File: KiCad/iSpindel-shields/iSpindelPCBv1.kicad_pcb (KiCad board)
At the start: 2 copper layers, 60 x 25 mm, 9 parts, among them SW1 SW_DPDT_x2, U1 GY-521, U2 LoRa_Ra-02, U3 WeMos_mini, U4 TP4056-shield-6PIN, U5 DS18B20

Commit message: adjust switch and charger
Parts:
- added SW2: SW_SPDT, KiCadCustomLibs:SS-12F23, F.Cu at (152.8, 112.5)
- SW1: value SW_DPDT_x2 -> SW_SPDT
- moved U4 0.75 mm to (146.2, 112.5)
- moved SW1 0.50 mm to (157.5, 112.5)

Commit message: adjusted some tracks
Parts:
- SW2: footprint KiCadCustomLibs:SS-12F23 -> SS-12F23
- moved U3 4.00 mm to (148.0, 112.5)
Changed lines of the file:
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@@
     (add_net "Net-(U4-Pad4)")
   )
-  (module KiCadCustomLibs:SS-12F23 (layer F.Cu)
+  (module KiCadCustomLibs:TP4056-shield-6PIN (layer B.Cu)
+    (at 146.25 112.5 180)
+    (fp_text reference U4 (at 0.5 0 180) (layer B.SilkS) hide
+      (effects (font (size 1 1) (thickness 0.15)) (justify mirror))
+    )
+    (fp_text value TP4056-shield-6PIN (at 0 7 180) (layer B.Fab) hide
+      (effects (font (size 1 1) (thickness 0.15)) (justify mirror))
+    )
+    (fp_line (start -14.5 -4) (end -9.5 -4) (layer B.Fab) (width 0.15))
+    (fp_line (start 13 6) (end 13 -6) (layer B.SilkS) (width 0.15))
+    (fp_line (start 13 6) (end 14.5 6) (layer B.SilkS) (width 0.15))
+    (fp_line (start 14.5 6) (end 14.5 8.5) (layer B.SilkS) (width 0.15))
+    (fp_line (start 14.5 8.5) (end 13.5 8.5) (layer B.SilkS) (width 0.15))
+    (fp_line (start 13 -6) (end 14.5 -6) (layer B.SilkS) (width 0.15))
+    (fp_line (start 14.5 -6) (end 14.5 -8.5) (layer B.SilkS) (width 0.15))
+    (fp_line (start 14.5 -8.5) (end 13.5 -8.5) (layer B.SilkS) (width 0.15))
+    (fp_line (start -9.5 -4) (end -9.5 4) (layer B.Fab) (width 0.15))
+    (fp_line (start -9.5 4) (end -14.5 4) (layer B.Fab) (width 0.15))
+    (fp_line (start -14.5 4) (end -14.5 -4) (layer B.Fab) (width 0.15))
+    (fp_line (start -13.5 -8.5) (end -13.5 8.5) (layer B.SilkS) (width 0.15))
+    (fp_line (start -13.5 8.5) (end 13.5 8.5) (layer B.SilkS) (width 0.15))
+    (fp_line (start 13.5 -8.5) (end -13.5 -8.5) (layer B.SilkS) (width 0.15))
+    (pad 3 thru_hole oval (at 11.1 7 180) (size 3 2) (drill 1) (layers *.Cu *.Mask)
+      (net 6 "Net-(SW1-Pad1)"))
+    (pad 4 thru_hole oval (at 11.1 -7 180) (size 3 2) (drill 1) (layers *.Cu *.Mask)
+      (net 28 "Net-(U4-Pad4)"))
+    (pad 2 thru_hole oval (at -11.5 -7 180) (size 3 2) (drill 1) (layers *.Cu B.Mask)
+      (net 13 GND))
+    (pad 1 thru_hole oval (at -11.5 7 180) (size 3 2) (drill 1) (layers *.Cu B.Mask)
+      (net 30 "Net-(U4-Pad1)"))
+    (model ../../../../../../src/Tennp/Git/KiCadCustomLibs/wrl/TP4056shield.wrl
+      (at (xyz 0 0 0))
+      (scale (xyz 0.395 0.395 0.395))
+      (rotate (xyz 0 0 180))
+    )
+    (model ../../../../../../src/Tennp/Git/KiCadCustomLibs/wrl/Conn_USB-micro-2.0_socket_right-angle.wrl
+      (at (xyz -0.47 0 0.047))
+      (scale (xyz 1 1 1))
+      (rotate (xyz 0 0 0))
+    )
+  )
+  (module SS-12F23 (layer F.Cu)
     (at 152.75 112.5 270)
     (fp_text reference SW2 (at 0.5 -2 270) (layer F.SilkS) hide
@@
     (pad 2 thru_hole circle (at 0 0 270) (size 2 2) (drill 1) (layers *.Cu *.Mask)
       (net 3 +5V))
+    (model ../../../../../../src/Tennp/Git/KiCadCustomLibs/wrl/SS-12F23.wrl
+      (at (xyz 0 0.12 0))
+      (scale (xyz 0.395 0.395 0.395))
+      (rotate (xyz 0 0 180))
+    )
   )
   (module wemos_D1_mini_board (layer F.Cu)
-    (at 144 112.5 90)
+    (at 148 112.5 90)
     (fp_text reference U3 (at -10.668 14.224 90) (layer F.SilkS)
       (effects (font (size 1 1) (thickness 0.15)))
@@
       (rotate (xyz 0 0 0))
     )
-  )
-  (module KiCadCustomLibs:TP4056-shield-6PIN (layer B.Cu)
-    (at 146.25 112.5 180)
-    (fp_text reference U4 (at 0.5 0 180) (layer B.SilkS)
-      (effects (font (size 1 1) (thickness 0.15)) (justify mirror))
-    )
-    (fp_text value TP4056-shield-6PIN (at 0 7 180) (layer B.Fab) hide
-      (effects (font (size 1 1) (thickness 0.15)) (justify mirror))
-    )
-    (fp_line (start -14.5 -4) (end -9.5 -4) (layer B.Fab) (width 0.15))
-    (fp_line (start 13 6) (end 13 -6) (layer B.SilkS) (width 0.15))
-    (fp_line (start 13 6) (end 14.5 6) (layer B.SilkS) (width 0.15))
-    (fp_line (start 14.5 6) (end 14.5 8.5) (layer B.SilkS) (width 0.15))
-    (fp_line (start 14.5 8.5) (end 13.5 8.5) (layer B.SilkS) (width 0.15))
-    (fp_line (start 13 -6) (end 14.5 -6) (layer B.SilkS) (width 0.15))
-    (fp_line (start 14.5 -6) (end 14.5 -8.5) (layer B.SilkS) (width 0.15))
-    (fp_line (start 14.5 -8.5) (end 13.5 -8.5) (layer B.SilkS) (width 0.15))
-    (fp_line (start -9.5 -4) (end -9.5 4) (layer B.Fab) (width 0.15))
-    (fp_line (start -9.5 4) (end -14.5 4) (layer B.Fab) (width 0.15))
-    (fp_line (start -14.5 4) (end -14.5 -4) (layer B.Fab) (width 0.15))
-    (fp_line (start -13.5 -8.5) (end -13.5 8.5) (layer B.SilkS) (width 0.15))
-    (fp_line (start -13.5 8.5) (end 13.5 8.5) (layer B.SilkS) (width 0.15))
-    (fp_line (start 13.5 -8.5) (end -13.5 -8.5) (layer B.SilkS) (width 0.15))
-    (pad 3 thru_hole oval (at 11.1 7 180) (size 3 2) (drill 1) (layers *.Cu *.Mask)
-      (net 6 "Net-(SW1-Pad1)"))
-    (pad 4 thru_hole oval (at 11.1 -7 180) (size 3 2) (drill 1) (layers *.Cu *.Mask)
-      (net 28 "Net-(U4-Pad4)"))
-    (pad 2 thru_hole oval (at -11.5 -7 180) (size 3 2) (drill 1) (layers *.Cu *.Mask)
-      (net 13 GND))
-    (pad 1 thru_hole oval (at -11.5 7 180) (size 3 2) (drill 1) (layers *.Cu *.Mask)
-      (net 30 "Net-(U4-Pad1)"))
-    (model ../../../../../../src/Tennp/Git/KiCadCustomLibs/wrl/TP4056shield.wrl
-      (at (xyz 0 0 0))
-      (scale (xyz 0.395 0.395 0.395))
-      (rotate (xyz 0 0 180))
-    )
-    (model ../../../../../../src/Tennp/Git/KiCadCustomLibs/wrl/Conn_USB-micro-2.0_socket_right-angle.wrl
-      (at (xyz -0.47 0 0.047))
-      (scale (xyz 1 1 1))
-      (rotate (xyz 0 0 0))
-    )

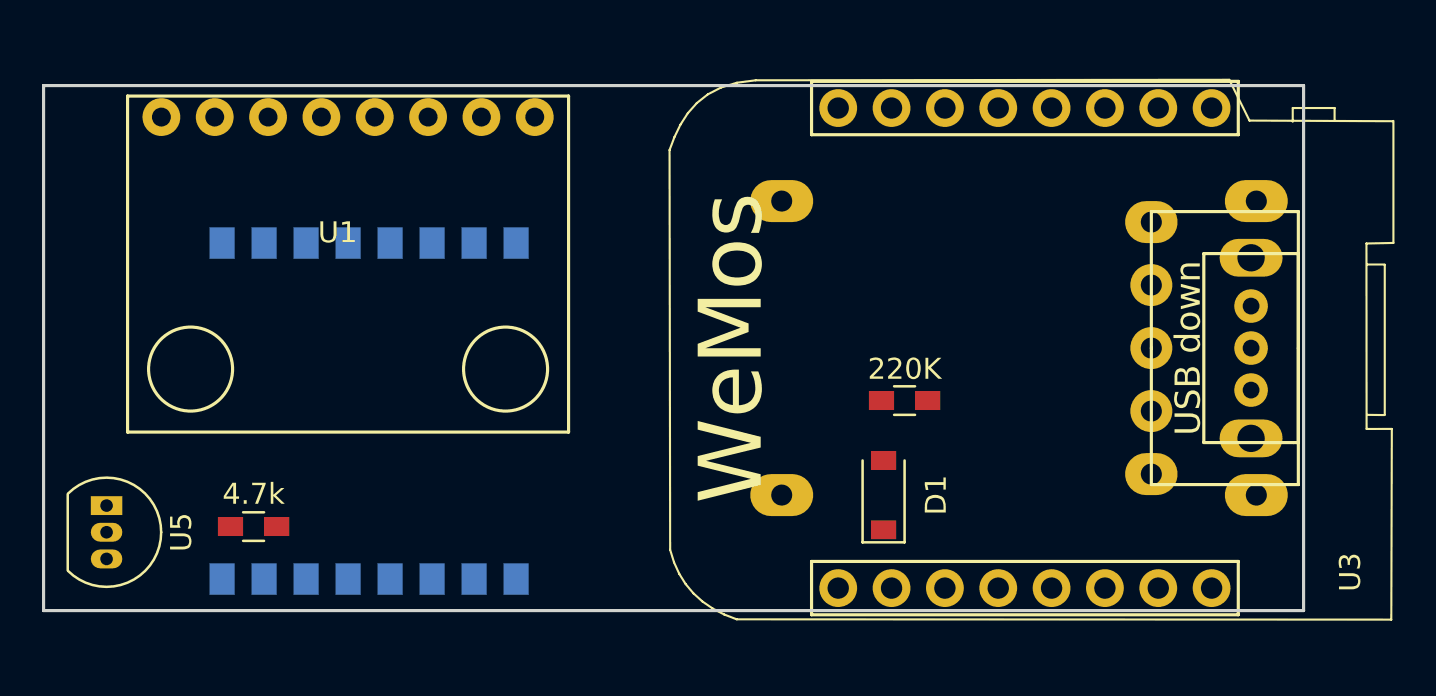
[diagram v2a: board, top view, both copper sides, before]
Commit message: Add TH variant
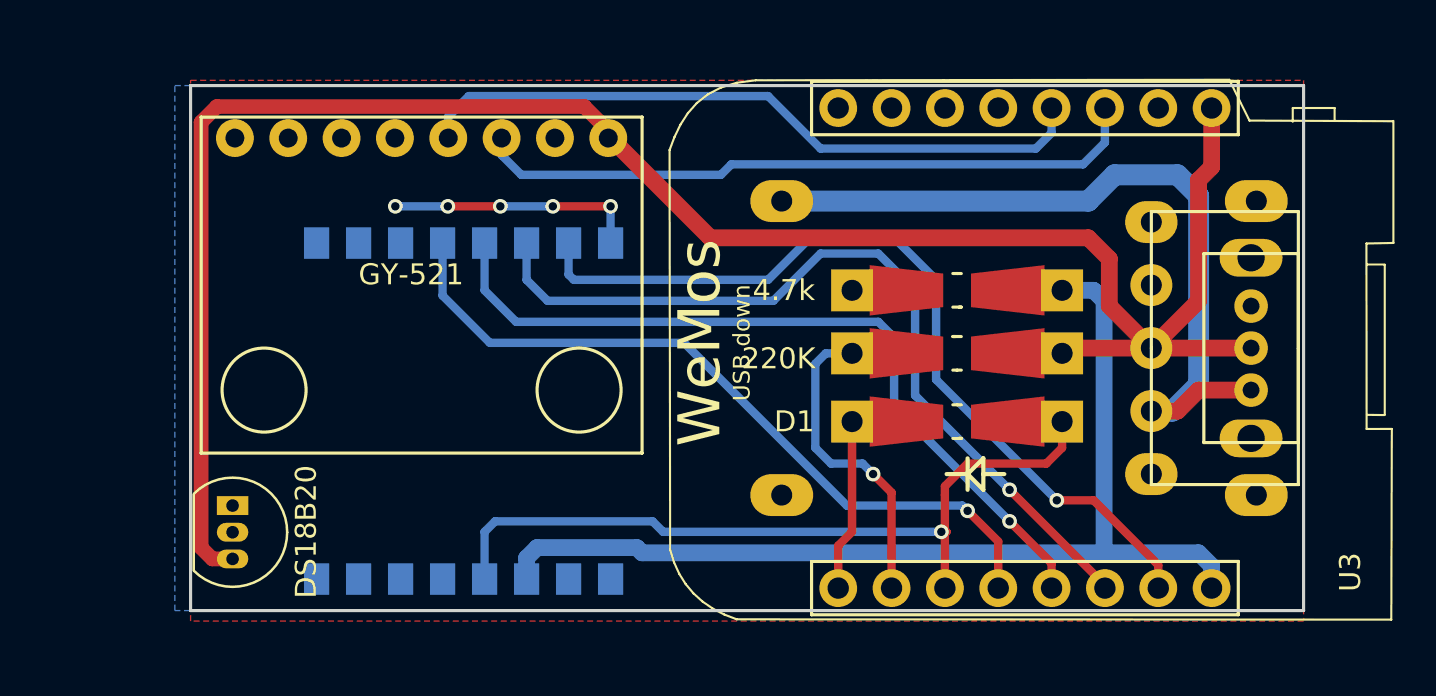
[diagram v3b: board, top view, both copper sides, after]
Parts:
- D1: footprint Diodes_SMD:D_SOD-123 -> Resistors_Universal:Resistor_SMD+THTuniversal_0805to1206_RM10_HandSoldering
- R1, R2: footprint Resistors_SMD:R_0603_HandSoldering -> Resistors_Universal:Resistor_SMD+THTuniversal_0805to1206_RM10_HandSoldering
- moved R2 35.3 mm to (143.5, 109.8)
- moved U5 6.00 mm to (109.0, 120.0)
- moved D1 4.95 mm to (143.5, 116.0), turned to 180 degrees
- moved U2 4.50 mm to (120.0, 115.5)
- moved U1 3.64 mm to (118.0, 109.5)
- moved R1 3.36 mm to (143.5, 112.8)
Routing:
- net +5V: track 0.00 -> 98.4 mm
- net +3V3: track 0.00 -> 52.0 mm
- net /NSS: track 0.00 -> 40.8 mm, vias 0 -> 1
- net /MOSI: track 0.00 -> 40.2 mm, vias 0 -> 1
- net /RES: track 0.00 -> 39.8 mm, vias 0 -> 1
- net Net-(SW1-Pad1): track 0.00 -> 38.2 mm
- net /MISO: track 0.00 -> 37.7 mm, vias 0 -> 1
- net /SCK: track 0.00 -> 36.0 mm, vias 0 -> 1
- net /SDA: track 0.00 -> 32.7 mm
- net /SCL: track 0.00 -> 32.2 mm
- net Net-(R1-Pad1): track 0.00 -> 17.6 mm, vias 0 -> 1
- net GND: track 0.00 -> 12.6 mm, vias 0 -> 5
- net Net-(D1-Pad2): track 0.00 -> 10.8 mm
- net /Temp: track 0.00 -> 2.59 mm
- added copper zone on B.Cu, net GND
- added copper zone on F.Cu, net GND
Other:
- board size 60 x 25 mm -> 53 x 25 mm
- net class Default: trace_width 0.25 -> 0.4; via_dia 0.6 -> 0.7
- net class POWER added: clearance 0.2, trace_width 0.8, via_dia 1, via_drill 0.5
- board text added: "Charger"
- board text added: "DS18B20"
- board text added: "LoRa Ra-02"

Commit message: Last changes
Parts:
- added REF**: SolderWirePad_single_SMD_5x10mm, Wire_Pads:SolderWirePad_single_SMD_5x10mm, F.Cu at (125.5, 114.5)
- added REF**: SolderWirePad_single_SMD_5x10mm, Wire_Pads:SolderWirePad_single_SMD_5x10mm, F.Cu at (110.5, 114.5)
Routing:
- net GND: track 12.6 -> 101.5 mm, vias 5 -> 31
- net /Temp: track 2.59 -> 60.3 mm, vias 0 -> 2
- net /MOSI: track 40.2 -> 36.5 mm
- net /MISO: track 37.7 -> 36.0 mm
- net /SCL: track 32.2 -> 33.4 mm
- net Net-(R1-Pad1): track 17.6 -> 18.8 mm, vias 1 -> 0
- net /NSS: track 40.8 -> 39.7 mm
- net /RES: track 39.8 -> 39.1 mm
- net Net-(D1-Pad2): track 10.8 -> 11.0 mm, vias 0 -> 1
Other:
- rule pad_to_mask_clearance: 0.2 -> 0.1
- board text added: "www.ispindel.de"

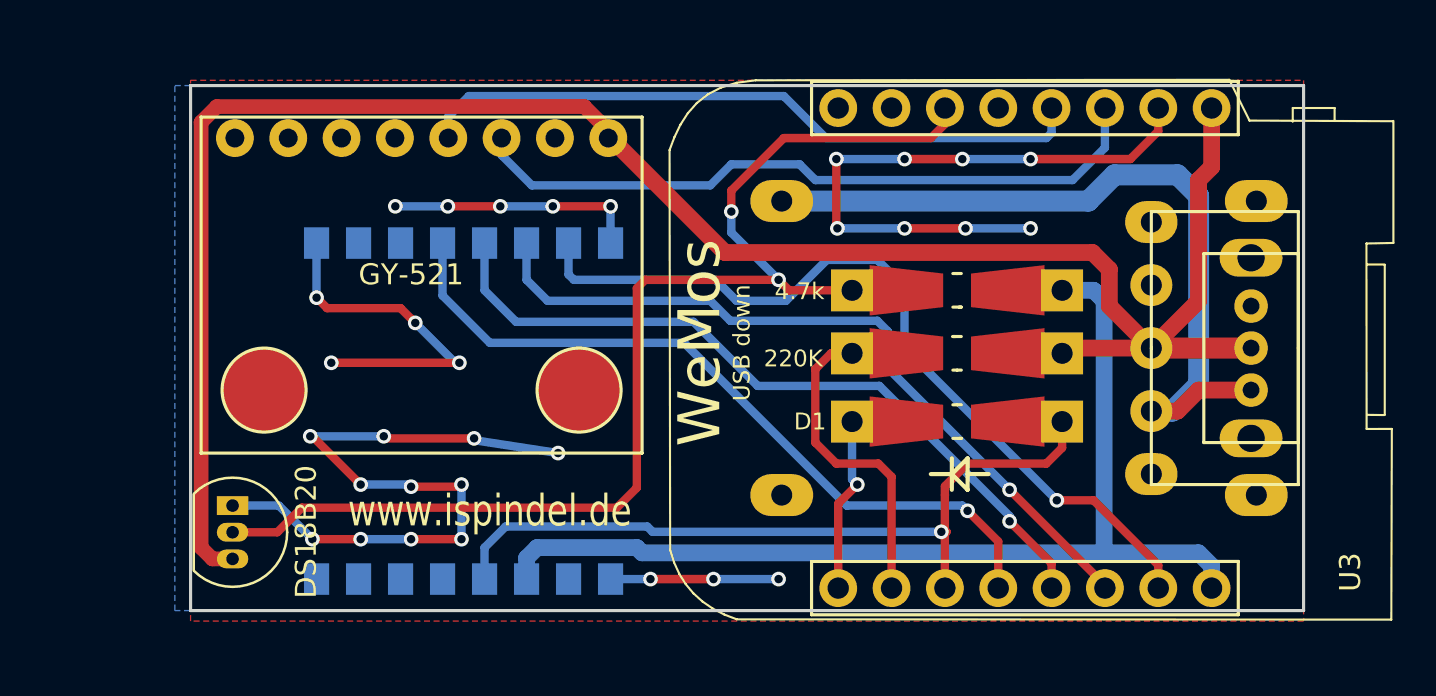
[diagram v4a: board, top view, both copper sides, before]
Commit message: Some minor adjustments to PCB. Added capacitor to DS
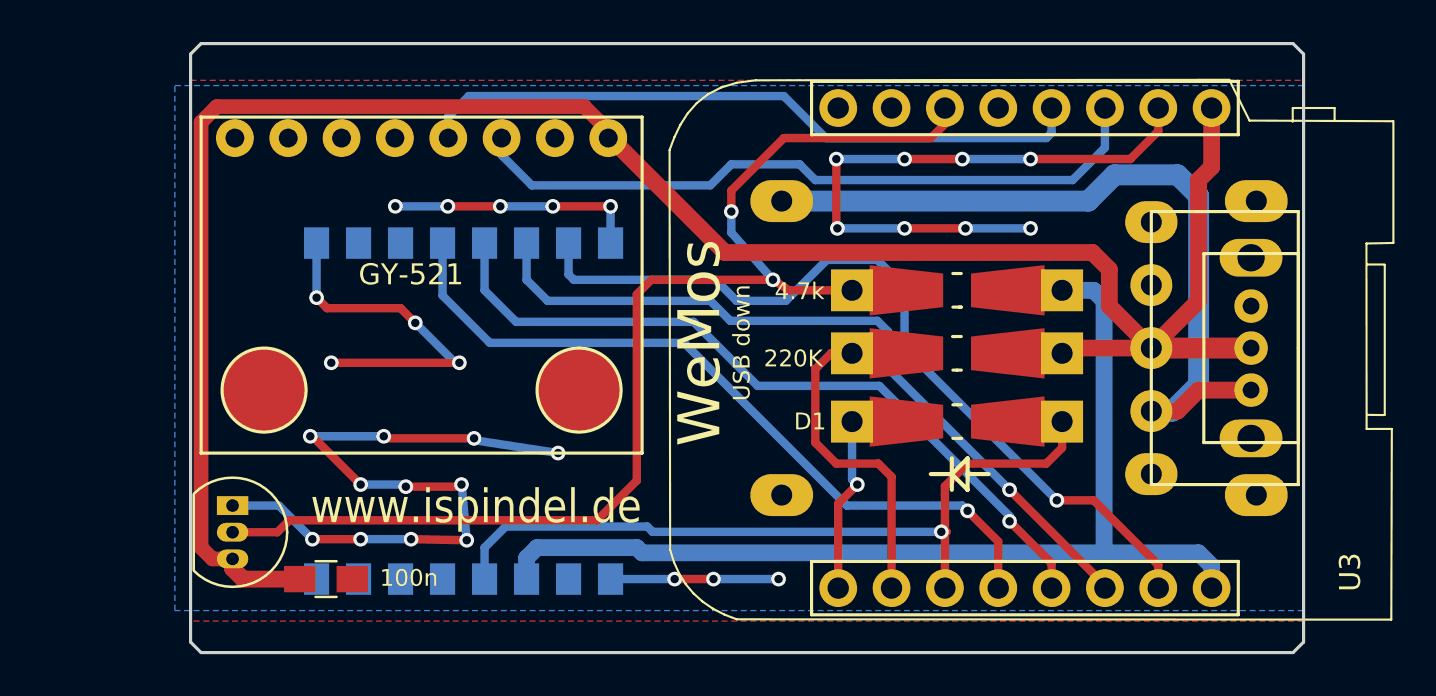
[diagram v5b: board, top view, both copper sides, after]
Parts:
- added C1: 100n, Capacitors_SMD:C_0805_HandSoldering, F.Cu at (113.5, 123.5)
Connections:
- SW1 pad 3: Net-(SW1-Pad3) -> (no net)
- SW2 pad 3: Net-(SW2-Pad3) -> (no net)
- U1 pad 5: Net-(U1-Pad5) -> (no net)
- U1 pad 6: Net-(U1-Pad6) -> (no net)
- U1 pad 7: Net-(U1-Pad7) -> (no net)
- U1 pad 8: Net-(U1-Pad8) -> (no net)
- U2 pad 10: Net-(U2-Pad10) -> (no net)
- U2 pad 11: Net-(U2-Pad11) -> (no net)
- U2 pad 5: Net-(U2-Pad5) -> (no net)
- U2 pad 6: Net-(U2-Pad6) -> (no net)
- U2 pad 7: Net-(U2-Pad7) -> (no net)
- U2 pad 8: Net-(U2-Pad8) -> (no net)
- U3 pad 5: Net-(U3-Pad5) -> (no net)
- U3 pad 7: Net-(U3-Pad7) -> (no net)
- U3 pad 8: Net-(U3-Pad8) -> (no net)
- U4 pad 1: Net-(U4-Pad1) -> (no net)
- U4 pad 4: Net-(U4-Pad4) -> (no net)
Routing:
- net +5V: track 98.1 -> 102.0 mm
- net /Temp: track 60.3 -> 59.7 mm
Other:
- board size 53 x 25 mm -> 53 x 29 mm
